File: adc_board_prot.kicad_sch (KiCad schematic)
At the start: 0 parts

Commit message: Change detector connector
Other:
- company: (none) -> NOIRLab
- title: (none) -> 4 channel ADC Module
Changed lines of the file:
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@@
 	(generator_version "9.0")
 	(paper "A4")
+	(title_block
+		(title "4 channel ADC Module")
+		(date "2025-04-18")
+		(rev "0.1")
+		(company "NOIRLab")
+		(comment 1 "Design: Braulio Cancino Vera - braulio.cancino@noirlab.edu")
+	)
 	(sheet
 		(at 104.14 35.56)

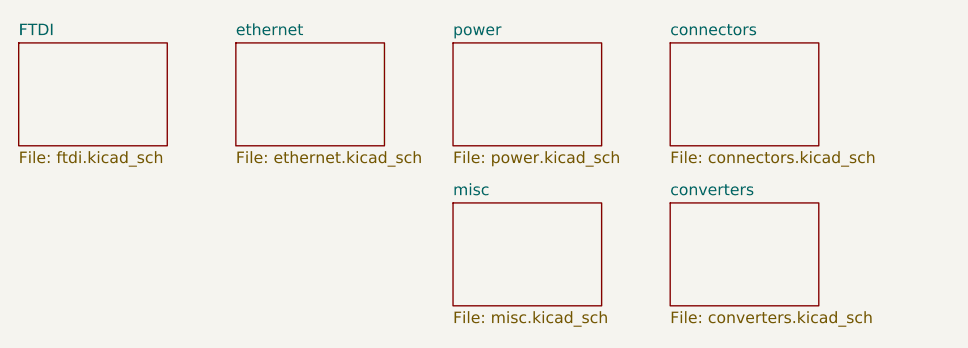
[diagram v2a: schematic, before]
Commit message: Added clock sync and fix minor errors.
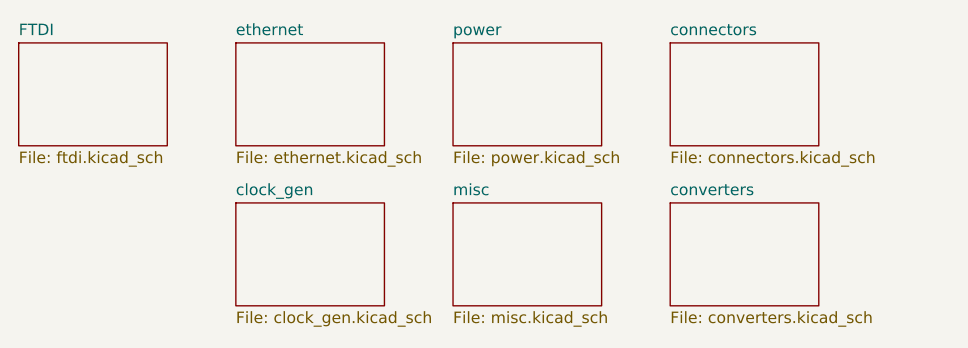
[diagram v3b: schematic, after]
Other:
- added sheet clock_gen (clock_gen.kicad_sch)
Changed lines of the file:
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@@
 	(title_block
 		(title "4 channel ADC Module")
-		(date "2025-04-18")
+		(date "2025-05-06")
 		(rev "0.1")
 		(company "NOIRLab")
@@
 			(project "adc_board_prot"
 				(path "/c6949a33-abae-4c95-a3fe-c6f7de9ef0a5"
-					(page "4")
+					(page "15")
 				)
 			)
@@
 			(project "adc_board_prot"
 				(path "/c6949a33-abae-4c95-a3fe-c6f7de9ef0a5"
-					(page "3")
+					(page "8")
 				)
 			)
@@
 			(project "adc_board_prot"
 				(path "/c6949a33-abae-4c95-a3fe-c6f7de9ef0a5"
-					(page "14")
+					(page "9")
 				)
 			)
@@
 			(project "adc_board_prot"
 				(path "/c6949a33-abae-4c95-a3fe-c6f7de9ef0a5"
-					(page "2")
+					(page "7")
+				)
+			)
+		)
+	)
+	(sheet
+		(at 80.01 53.34)
+		(size 16.51 11.43)
+		(exclude_from_sim no)
+		(in_bom yes)
+		(on_board yes)
+		(dnp no)
+		(fields_autoplaced yes)
+		(stroke
+			(width 0.1524)
+			(type solid)
+		)
+		(fill
+			(color 0 0 0 0.0000)
+		)
+		(property "Sheetname" "clock_gen"
+			(at 80.01 52.6284 0)
+			(effects
+				(font
+					(size 1.27 1.27)
+				)
+				(justify left bottom)
+			)
+		)
+		(property "Sheetfile" "clock_gen.kicad_sch"
+			(at 80.01 65.3546 0)
+			(effects
+				(font
+					(size 1.27 1.27)
+				)
+				(justify left top)
+			)
+		)
+		(instances
+			(project "adc_board_prot"
+				(path "/c6949a33-abae-4c95-a3fe-c6f7de9ef0a5"
+					(page "6")
 				)
 			)
@@
 			(project "adc_board_prot"
 				(path "/c6949a33-abae-4c95-a3fe-c6f7de9ef0a5"
-					(page "19")
+					(page "2")
 				)
 			)
@@
 			(project "adc_board_prot"
 				(path "/c6949a33-abae-4c95-a3fe-c6f7de9ef0a5"
-					(page "23")
-				)
-			)
+					(page "14")
+				)
+			)
